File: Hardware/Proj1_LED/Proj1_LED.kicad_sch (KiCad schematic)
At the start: 4 parts, among them J1 Conn_01x02, SW1 SW_Push

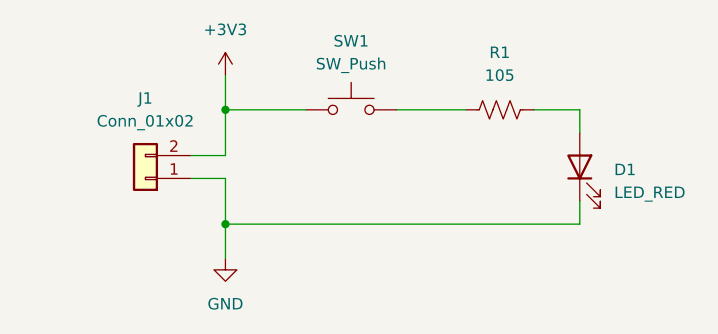
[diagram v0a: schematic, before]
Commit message: add PWR_FLAGS for schematic DRC
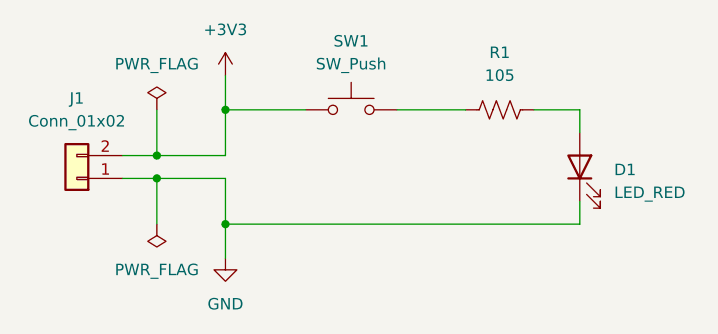
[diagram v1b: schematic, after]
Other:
- moved on the sheet: J1
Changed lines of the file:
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@@
+	)
+	(junction
+		(at 110.49 101.6)
+		(diameter 0)
+		(color 0 0 0 0)
 	)
 	(junction
@@
 	)
 	(junction
+		(at 110.49 99.06)
+		(diameter 0)
+		(color 0 0 0 0)
+	)
+	(junction
 		(at 118.11 106.68)
 		(diameter 0)
@@
 	(wire
 		(pts
+			(xy 110.49 101.6) (xy 110.49 106.68)
+		)
+		(stroke
+			(width 0)
+			(type default)
+		)
+	)
+	(wire
+		(pts
 			(xy 157.48 93.98) (xy 152.4 93.98)
 		)
@@
 	(wire
 		(pts
+			(xy 110.49 93.98) (xy 110.49 99.06)
+		)
+		(stroke
+			(width 0)
+			(type default)
+		)
+	)
+	(wire
+		(pts
 			(xy 157.48 104.14) (xy 157.48 106.68)
 		)
@@
 	(wire
 		(pts
-			(xy 114.3 99.06) (xy 118.11 99.06)
-		)
-		(stroke
-			(width 0)
-			(type default)
-		)
-	)
-	(wire
-		(pts
-			(xy 118.11 101.6) (xy 114.3 101.6)
+			(xy 106.68 99.06) (xy 110.49 99.06)
+		)
+		(stroke
+			(width 0)
+			(type default)
+		)
+	)
+	(wire
+		(pts
+			(xy 110.49 101.6) (xy 118.11 101.6)
+		)
+		(stroke
+			(width 0)
+			(type default)
+		)
+	)
+	(wire
+		(pts
+			(xy 106.68 101.6) (xy 110.49 101.6)
 		)
 		(stroke
@@
 		(pts
 			(xy 157.48 106.68) (xy 118.11 106.68)
+		)
+		(stroke
+			(width 0)
+			(type default)
+		)
+	)
+	(wire
+		(pts
+			(xy 110.49 99.06) (xy 118.11 99.06)
 		)
 		(stroke
@@
 	(symbol
 		(lib_id "Connector_Generic:Conn_01x02")
-		(at 109.22 101.6 180)
+		(at 101.6 101.6 180)
 		(unit 1)
 		(exclude_from_sim no)
@@
 		(fields_autoplaced yes)
 		(property "Reference" "J1"
-			(at 109.22 92.71 0)
+			(at 101.6 92.71 0)
 			(effects
 				(font
@@
 		)
 		(property "Value" "Conn_01x02"
-			(at 109.22 95.25 0)
+			(at 101.6 95.25 0)
 			(effects
 				(font
@@
 		)
 		(property "Footprint" "Connector_Molex:Molex_KK-254_AE-6410-02A_1x02_P2.54mm_Vertical"
-			(at 109.22 101.6 0)
+			(at 101.6 101.6 0)
 			(effects
 				(font
@@
 		)
 		(property "Datasheet" "https://www.molex.com/content/dam/molex/molex-dot-com/products/automated/en-us/salesdrawingpdf/641/6410/022272021_sd.pdf?inline"
-			(at 109.22 101.6 0)
+			(at 101.6 101.6 0)
 			(effects
 				(font
@@
 		)
 		(property "Description" "Generic connector, single row, 01x02, script generated (kicad-library-utils/schlib/autogen/connector/)"
-			(at 109.22 101.6 0)
+			(at 101.6 101.6 0)
 			(effects
 				(font
@@
 		)
 		(property "MPN" "022272021"
-			(at 109.22 101.6 0)
+			(at 101.6 101.6 0)
 			(effects
 				(font
@@
 		)
 		(property "Notes" ""
-			(at 109.22 101.6 0)
+			(at 101.6 101.6 0)
 			(effects
 				(font
@@
 	)
 	(symbol
+		(lib_id "power:PWR_FLAG")
+		(at 110.49 106.68 180)
+		(unit 1)
+		(exclude_from_sim no)
+		(in_bom yes)
+		(on_board yes)
+		(dnp no)
+		(fields_autoplaced yes)
+		(property "Reference" "#FLG02"
+			(at 110.49 108.585 0)
+			(effects
+				(font
+					(size 1.27 1.27)
+				)
+				(hide yes)
+			)
+		)
+		(property "Value" "PWR_FLAG"
+			(at 110.49 111.76 0)
+			(effects
+				(font
+					(size 1.27 1.27)
+				)
+			)
+		)
+		(property "Footprint" ""
+			(at 110.49 106.68 0)
+			(effects
+				(font
+					(size 1.27 1.27)
+				)
+				(hide yes)
+			)
+		)
+		(property "Datasheet" "~"
+			(at 110.49 106.68 0)
+			(effects
+				(font
+					(size 1.27 1.27)
+				)
+				(hide yes)
+			)
+		)
+		(property "Description" "Special symbol for telling ERC where power comes from"
+			(at 110.49 106.68 0)
+			(effects
+				(font
+					(size 1.27 1.27)
+				)
+				(hide yes)
+			)
+		)
+		(pin "1"
+		)
+		(instances
+			(project "Proj1_LED"
+				(path "/1e1b062d-fad0-427c-a622-c5b8a80b5268"
+					(reference "#FLG02")
+					(unit 1)
+				)
+			)
+		)
+	)
+	(symbol
 		(lib_id "power:+3V3")
 		(at 118.11 90.17 0)
@@
 					(unit 1)
 				)
+			)
+		)
+	)
+	(symbol
+		(lib_id "power:PWR_FLAG")
+		(at 110.49 93.98 0)
+		(unit 1)
+		(exclude_from_sim no)
+		(in_bom yes)
+		(on_board yes)
+		(dnp no)
+		(fields_autoplaced yes)
+		(property "Reference" "#FLG01"
+			(at 110.49 92.075 0)
+			(effects
+				(font
+					(size 1.27 1.27)
+				)
+				(hide yes)
+			)
+		)
+		(property "Value" "PWR_FLAG"
+			(at 110.49 88.9 0)
+			(effects
+				(font
+					(size 1.27 1.27)
+				)
+			)
+		)
+		(property "Footprint" ""
+			(at 110.49 93.98 0)
+			(effects
+				(font
+					(size 1.27 1.27)
+				)
+				(hide yes)
+			)
+		)
+		(property "Datasheet" "~"
+			(at 110.49 93.98 0)
+			(effects
+				(font
+					(size 1.27 1.27)
+				)
+				(hide yes)
+			)
+		)
+		(property "Description" "Special symbol for telling ERC where power comes from"
+			(at 110.49 93.98 0)
+			(effects
+				(font
+					(size 1.27 1.27)
+				)
+				(hide yes)
+			)
+		)
+		(pin "1"
+		)
+		(instances
+			(project "Proj1_LED"
+				(path "/1e1b062d-fad0-427c-a622-c5b8a80b5268"
+					(reference "#FLG01")
+					(unit 1)
+				)
